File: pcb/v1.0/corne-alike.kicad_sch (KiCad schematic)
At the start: 46 parts, among them J1 Conn_01x02_Socket, SW1 SW_PUSH, SW10 SW_PUSH, SW11 SW_PUSH, SW12 SW_PUSH, SW13 SW_PUSH, SW14 SW_PUSH, SW15 SW_PUSH, SW16 SW_PUSH, SW17 SW_PUSH, SW18 SW_PUSH, SW19 SW_PUSH, SW2 SW_PUSH, SW20 SW_PUSH, SW21 SW_PUSH, SW3 SW_PUSH, SW4 SW_PUSH, SW5 SW_PUSH, SW6 SW_PUSH, SW7 SW_PUSH, SW8 SW_PUSH, SW9 SW_PUSH, U1 nice_nano

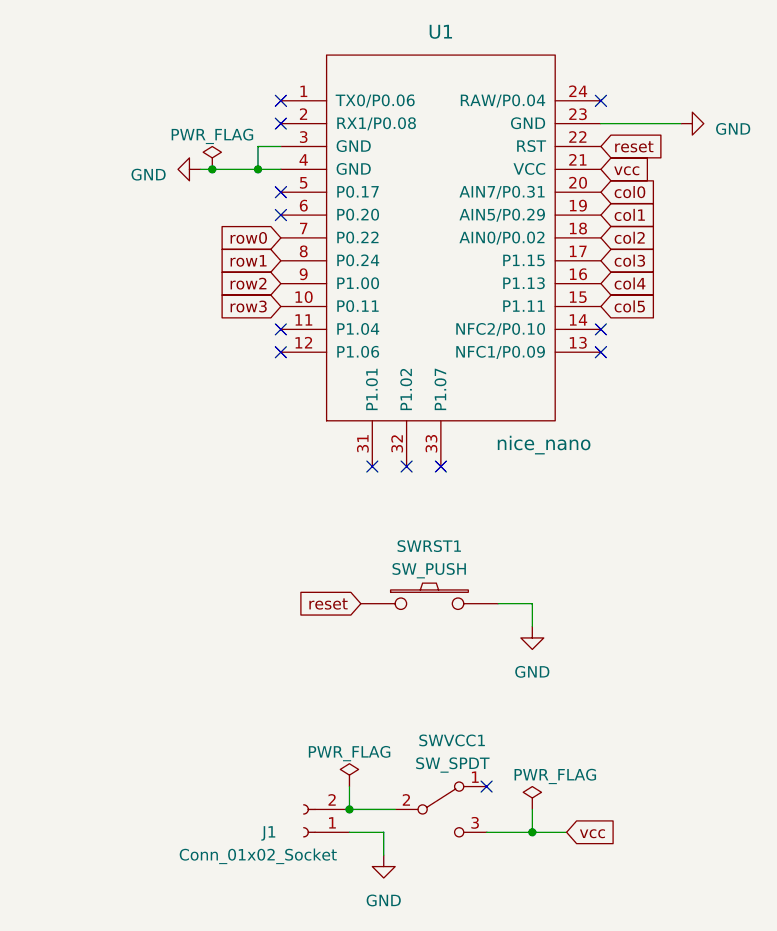
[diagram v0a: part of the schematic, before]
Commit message: Flip battery connector polarity, fix power input pin
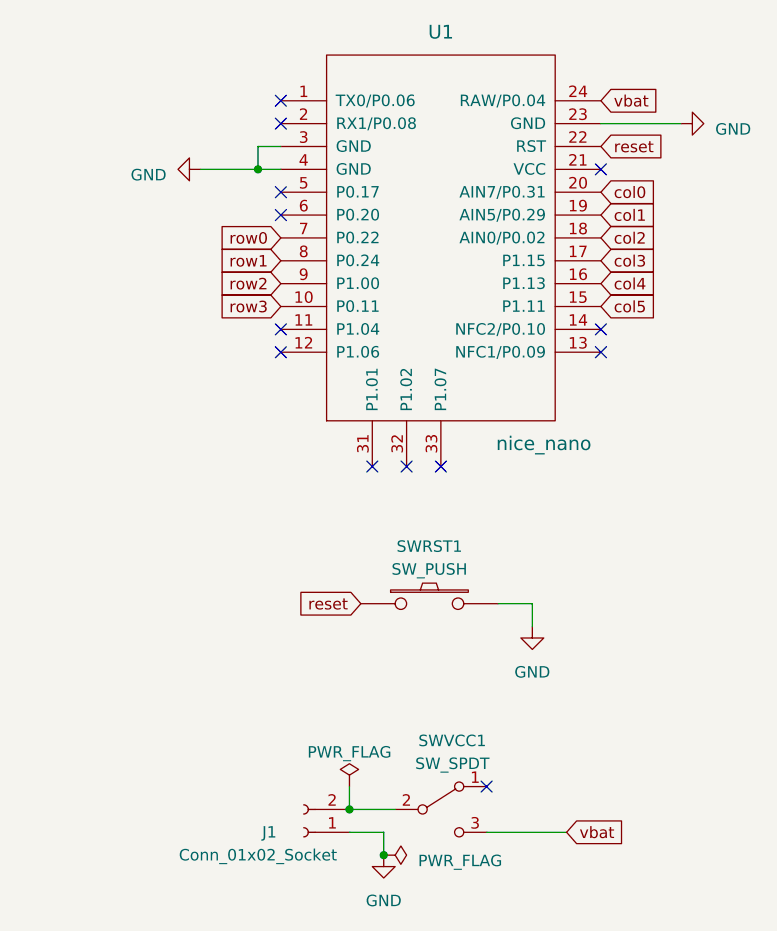
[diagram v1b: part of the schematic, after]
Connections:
- net vbat: now reaches U1.24 (RAW/P0.04)
- net vbat: now also SWVCC1.3 (C)
- net vcc: no longer names the net of U1.21 (VCC)
- net vcc: no longer SWVCC1.3 (C)
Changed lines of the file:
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@@
   (title_block
     (title "Corne alike keyboard")
-    (date "2023-02-15")
-    (rev "v1.0")
+    (date "2023-05-28")
+    (rev "v1.1")
     (comment 2 "https://github.com/rastasheep/corne-alike-kbd")
     (comment 3 "License: MIT (https://github.com/rastasheep/corne-alike-kbd/blob/main/LICENSE.md)")
@@
   (junction (at 124.46 38.1) (diameter 0) (color 0 0 0 0)
   )
-  (junction (at 209.55 30.48) (diameter 0) (color 0 0 0 0)
-  )
   (junction (at 95.25 87.63) (diameter 0) (color 0 0 0 0)
   )
@@
   (junction (at 99.06 57.15) (diameter 0) (color 0 0 0 0)
   )
+  (junction (at 228.6 106.68) (diameter 0) (color 0 0 0 0)
+  )
   (junction (at 95.25 67.31) (diameter 0) (color 0 0 0 0)
   )
@@
   )
   (junction (at 151.13 38.1) (diameter 0) (color 0 0 0 0)
-  )
-  (junction (at 245.11 104.14) (diameter 0) (color 0 0 0 0)
   )
   (junction (at 22.86 38.1) (diameter 0) (color 0 0 0 0)
@@
   (no_connect (at 252.73 48.26))
   (no_connect (at 217.17 48.26))
-  (no_connect (at 252.73 22.86))
   (no_connect (at 217.17 50.8))
   (no_connect (at 217.17 33.02))
@@
   (no_connect (at 217.17 25.4))
   (no_connect (at 217.17 22.86))
+  (no_connect (at 252.73 30.48))
   (no_connect (at 217.17 35.56))
   (no_connect (at 240.03 99.06))
   (no_connect (at 234.95 63.5))
   (no_connect (at 231.14 63.5))
-  (wire (pts (xy 209.55 30.48) (xy 214.63 30.48))
+  (wire (pts (xy 208.28 30.48) (xy 214.63 30.48))
     (stroke (width 0) (type default))
   )
@@
     (stroke (width 0) (type default))
   )
-  (wire (pts (xy 240.03 104.14) (xy 245.11 104.14))
+  (wire (pts (xy 240.03 104.14) (xy 248.92 104.14))
     (stroke (width 0) (type default))
   )
@@
     (stroke (width 0) (type default))
   )
-  (wire (pts (xy 208.28 30.48) (xy 209.55 30.48))
-    (stroke (width 0) (type default))
-  )
   (wire (pts (xy 142.24 76.2) (xy 147.32 76.2))
     (stroke (width 0) (type default))
@@
     (stroke (width 0) (type default))
   )
-  (wire (pts (xy 245.11 101.6) (xy 245.11 104.14))
-    (stroke (width 0) (type default))
-  )
   (wire (pts (xy 95.25 66.04) (xy 95.25 67.31))
     (stroke (width 0) (type default))
@@
     (stroke (width 0) (type default))
   )
-  (wire (pts (xy 245.11 104.14) (xy 248.92 104.14))
-    (stroke (width 0) (type default))
-  )
   (wire (pts (xy 217.17 27.94) (xy 214.63 27.94))
     (stroke (width 0) (type default))
@@
     (stroke (width 0) (type default))
   )
-  (global_label "vcc" (shape input) (at 248.92 104.14 0) (fields_autoplaced)
+  (global_label "vbat" (shape input) (at 248.92 104.14 0) (fields_autoplaced)
     (effects (font (size 1.27 1.27)) (justify left))
-    (property "Intersheetrefs" "${INTERSHEET_REFS}" (at 254.9706 104.14 0)
+    (property "Intersheetrefs" "${INTERSHEET_REFS}" (at 255.8171 104.14 0)
       (effects (font (size 1.27 1.27)) (justify left) hide)
     )
@@
     )
   )
-  (global_label "vcc" (shape input) (at 252.73 30.48 0) (fields_autoplaced)
-    (effects (font (size 1.27 1.27)) (justify left))
-    (property "Intersheetrefs" "${INTERSHEET_REFS}" (at 258.7806 30.48 0)
-      (effects (font (size 1.27 1.27)) (justify left) hide)
-    )
-  )
   (global_label "row1" (shape input) (at 25.4 67.31 180) (fields_autoplaced)
     (effects (font (size 1.27 1.27)) (justify right))
@@
     )
   )
+  (global_label "vbat" (shape input) (at 252.73 22.86 0) (fields_autoplaced)
+    (effects (font (size 1.27 1.27)) (justify left))
+    (property "Intersheetrefs" "${INTERSHEET_REFS}" (at 259.6271 22.86 0)
+      (effects (font (size 1.27 1.27)) (justify left) hide)
+    )
+  )
   (global_label "col5" (shape input) (at 151.13 29.21 90) (fields_autoplaced)
     (effects (font (size 1.27 1.27)) (justify left))
@@
     )
   )
-  (symbol (lib_id "power:PWR_FLAG") (at 209.55 30.48 0) (unit 1)
-    (in_bom yes) (on_board yes) (dnp no) (fields_autoplaced)
-    (property "Reference" "#FLG02" (at 209.55 28.575 0)
-      (effects (font (size 1.27 1.27)) hide)
-    )
-    (property "Value" "PWR_FLAG" (at 209.55 26.67 0)
-      (effects (font (size 1.27 1.27)))
-    )
-    (property "Footprint" "" (at 209.55 30.48 0)
-      (effects (font (size 1.27 1.27)) hide)
-    )
-    (property "Datasheet" "~" (at 209.55 30.48 0)
+  (symbol (lib_id "power:PWR_FLAG") (at 228.6 106.68 270) (unit 1)
+    (in_bom yes) (on_board yes) (dnp no) (fields_autoplaced)
+    (property "Reference" "#FLG02" (at 230.505 106.68 0)
+      (effects (font (size 1.27 1.27)) hide)
+    )
+    (property "Value" "PWR_FLAG" (at 232.41 107.315 90)
+      (effects (font (size 1.27 1.27)) (justify left))
+    )
+    (property "Footprint" "" (at 228.6 106.68 0)
+      (effects (font (size 1.27 1.27)) hide)
+    )
+    (property "Datasheet" "~" (at 228.6 106.68 0)
       (effects (font (size 1.27 1.27)) hide)
     )
@@
         )
       )
-    )
-  )
-  (symbol (lib_id "power:PWR_FLAG") (at 245.11 101.6 0) (unit 1)
-    (in_bom yes) (on_board yes) (dnp no)
-    (property "Reference" "#FLG03" (at 245.11 99.695 0)
-      (effects (font (size 1.27 1.27)) hide)
-    )
-    (property "Value" "PWR_FLAG" (at 247.65 97.79 0)
-      (effects (font (size 1.27 1.27)))
-    )
-    (property "Footprint" "" (at 245.11 101.6 0)
-      (effects (font (size 1.27 1.27)) hide)
-    )
-    (property "Datasheet" "~" (at 245.11 101.6 0)
-      (effects (font (size 1.27 1.27)) hide)
-    )
-    (pin "1")
-    (instances
-      (project "corne-alike"
-        (path "/0486ce6e-d8f4-41f3-afb2-9305d9ed90ac"
-          (reference "#FLG03") (unit 1)
-        )
-      )
